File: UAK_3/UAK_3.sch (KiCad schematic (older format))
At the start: 57 parts, among them K1 Кнопка_FSMSM, K2 Кнопка_FSMSM, X1 Крепежное_отверстие_М3, X2 Крепежное_отверстие_М3, X3 Крепежное_отверстие_М3, X4 Крепежное_отверстие_М3

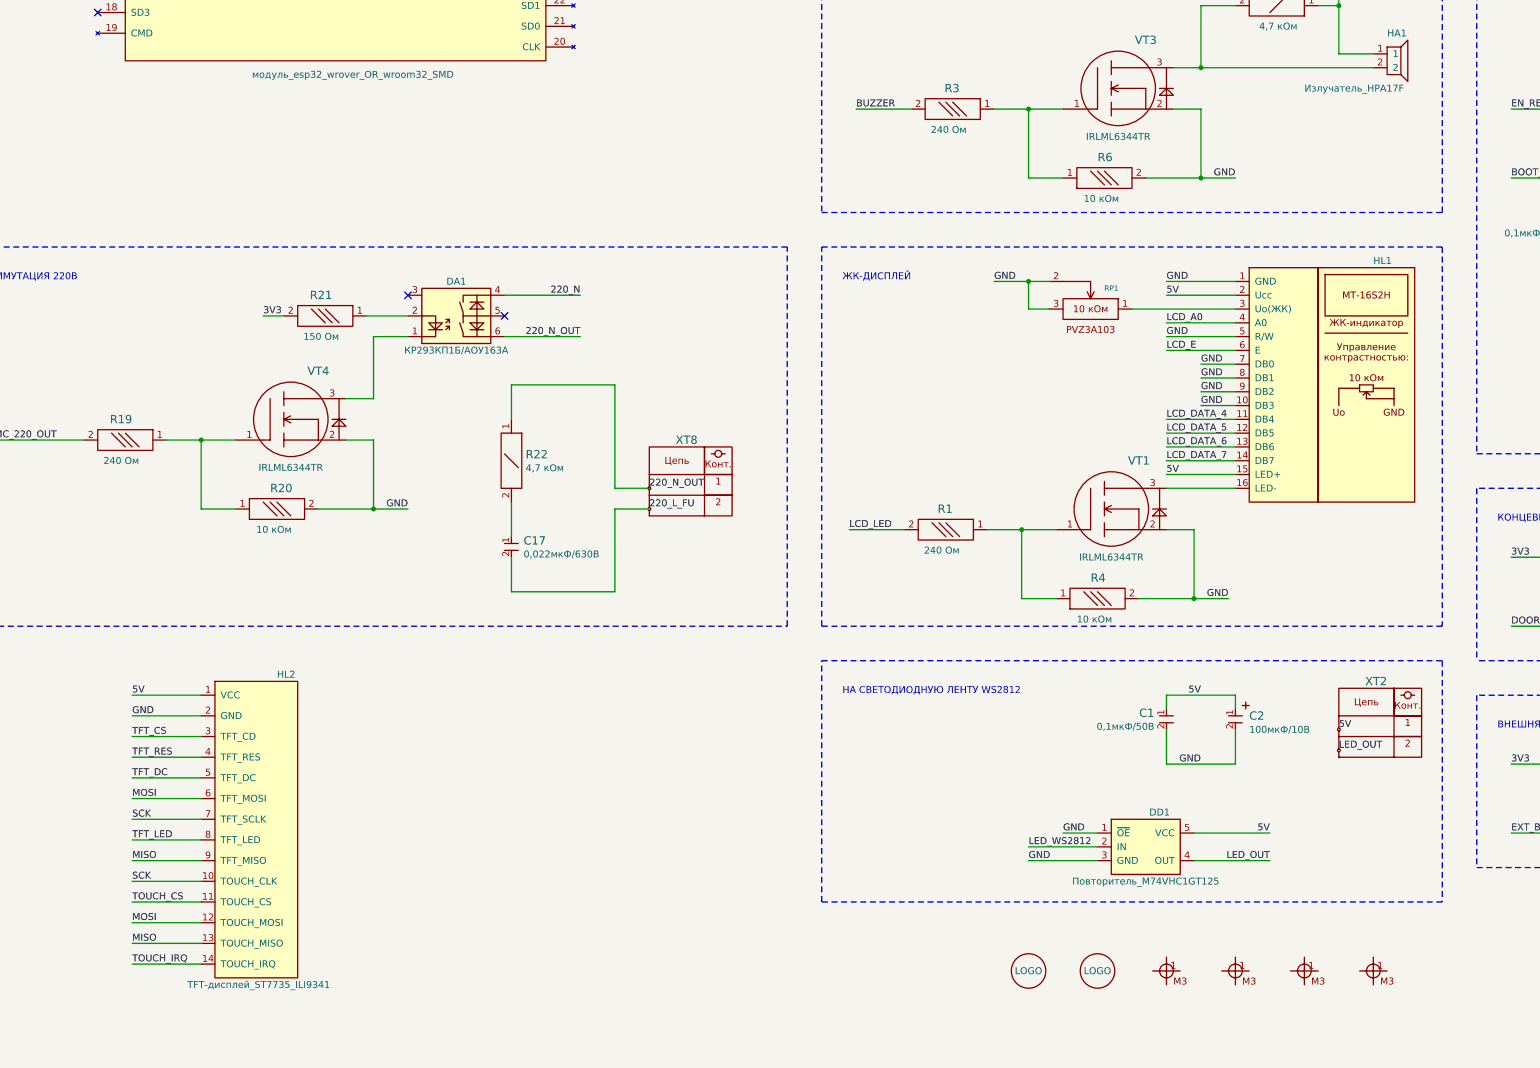
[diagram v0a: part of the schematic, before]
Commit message: добавлены сопротивления: в управление ЖК и выход 220
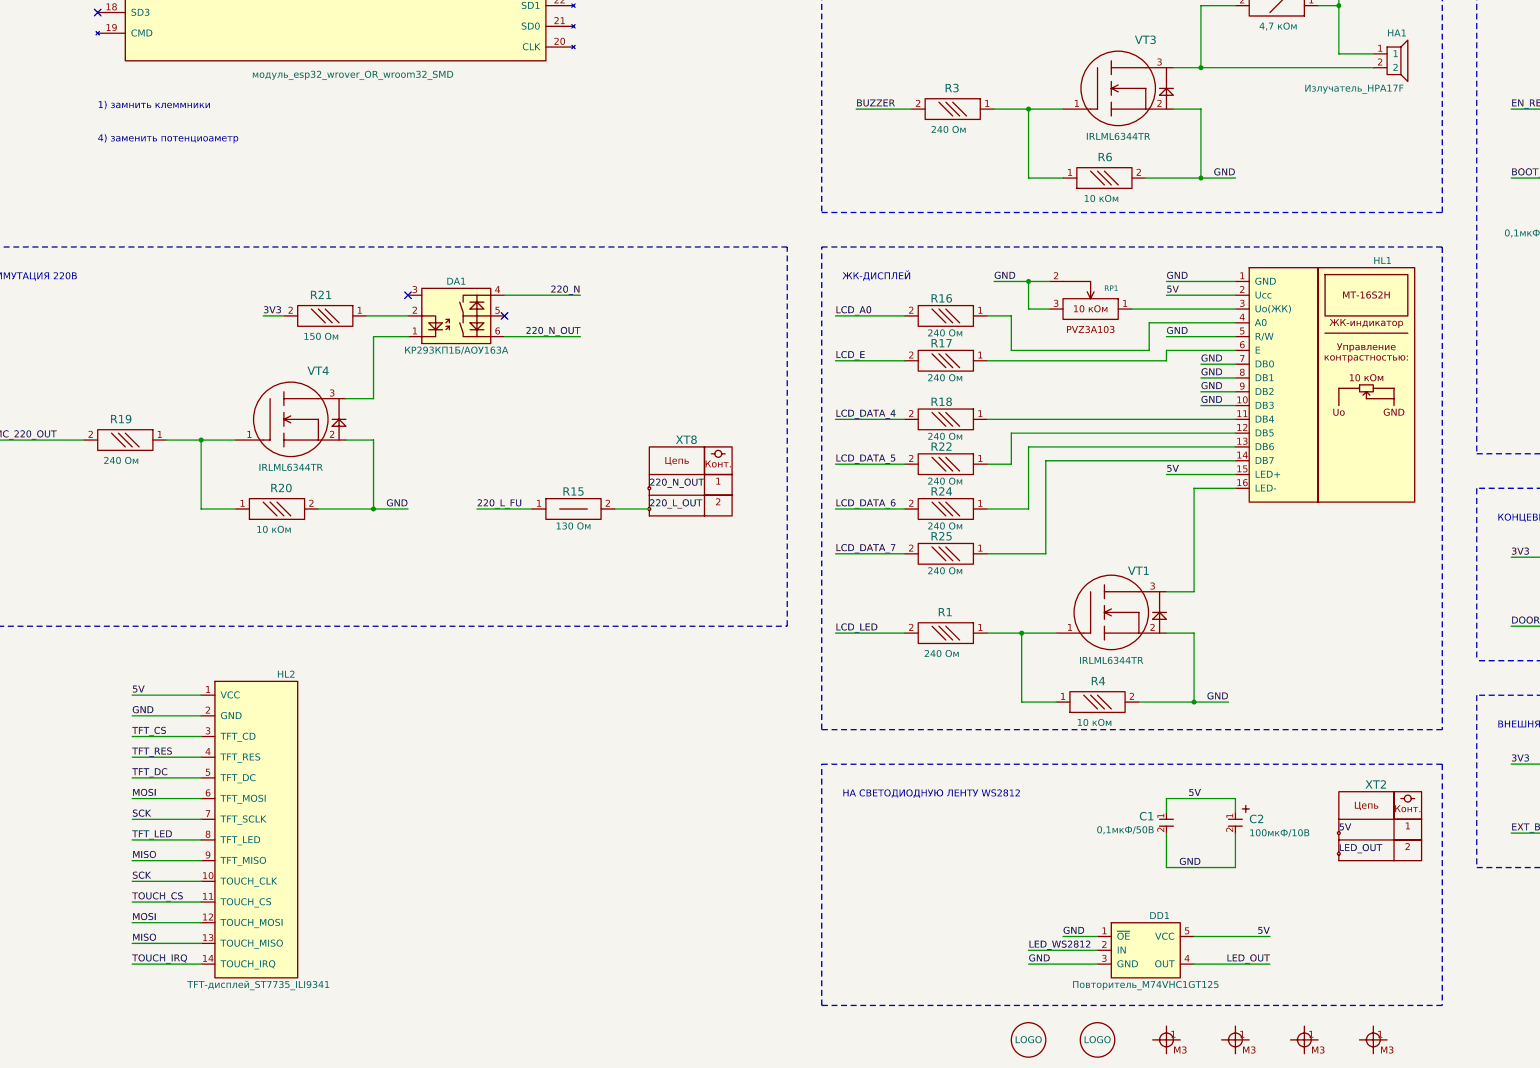
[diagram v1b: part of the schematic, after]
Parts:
- removed C17: Конденсатор_керамический, N_RLC:Конденсатор_SMD_1210, symbol elements:Конденсатор_керамический
- removed R22: Резистор_0,25Вт, N_RLC:Резистор_SMD_1206-0,25_Вт, symbol elements:Резистор_0,25Вт
- added R15: Резистор_0,5Вт, N_RLC:Резистор_SMD_2010-0,5_Вт, symbol elements:Резистор_0,5Вт
- added R16, R17, R18, R22, R24, R25: Резистор_0,065Вт, N_RLC:Резистор_SMD_0603_0,065_Вт, symbol elements:Резистор_0,065Вт
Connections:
- net 220_L_FU: now also R15.1; no longer XT8.2
- net LCD_A0: now also R16.2; no longer HL1.4 (A0)
- net LCD_DATA_4: now also R18.2; no longer HL1.11 (DB4)
- net LCD_DATA_5: now also R22.2; no longer HL1.12 (DB5)
- net LCD_DATA_6: now also R24.2; no longer HL1.13 (DB6)
- net LCD_DATA_7: now also R25.2; no longer HL1.14 (DB7)
- net LCD_E: now also R17.2; no longer HL1.6 (E)
- new net: HL1.11 (DB4), R18.1
- new net: HL1.12 (DB5), R22.1
- new net: HL1.13 (DB6), R24.1
- new net: HL1.14 (DB7), R25.1
- new net: HL1.4 (A0), R16.1
- new net: HL1.6 (E), R17.1
- new net 220_L_OUT: R15.2, XT8.2
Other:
- note added: "1) замнить клеммники\n\n\n4) заменить потенциоаметр"
- moved on the sheet: C1, C2, DD1, R1, R4, VT1, XT2

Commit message: заменены клеммники
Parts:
- removed XT1, XT2, XT3, XT6, XT7: Клеммник_х2_308-021-14, N_X:Клеммник_х2_шаг2.54, symbol UAK_3-rescue:Клеммник_х2_KLS2-300-5.00-02P-2S-elements_2020-UAK_0-rescue-UAK_1-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
- removed XT4, XT8: Клеммник_х2_KLS2-300-5.00-02P-2S, N_X:Клеммник_х2_шаг5, symbol UAK_3-rescue:Клеммник_х2_KLS2-300-5.00-02P-2S-elements_2020-UAK_0-rescue-UAK_1-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
- added X5: Клеммник_х4, N_X:Клеммник_х4_шаг3,81_15EDGRC, symbol elements:Клеммник_х4
- added X6: Клеммник_х10, N_X:Клеммник_х10_шаг3,81_15EDGRC, symbol elements:Клеммник_х10
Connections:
- net 220_L: now also X5.3
- net 220_L_OUT: now also X5.2
- net 220_N: now also X5.4
- net 220_N_OUT: now also X5.1
- net 5V: now also X6.3, X6.8, X6.9
- net BUTT_1: now also X6.6
- net DOOR_1: now also X6.1
- net D_OUT_1: now also X6.10
- net GND: now also X6.2, X6.5, X6.7
- net LED_OUT: now also X6.4
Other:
- note added: "4) заменить потенциометр"
- note added: "ПОДСВЕТКА ЛАМПЫ \n(ОТКРЫТЫЙ СТОК)"
- note removed: "1) замнить клеммники\n\n\n4) заменить потенциоаметр"
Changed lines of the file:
@@
 EESchema Schematic File Version 4
 LIBS:UAK_3-cache
-EELAYER 30 0
+EELAYER 29 0
 EELAYER END
 $Descr A3 16535 11693
@@
 	1    1950 1000
 	1    0    0    -1
-$EndComp
-$Comp
-L UAK_3-rescue:Клеммник_х2_KLS2-300-5.00-02P-2S-elements_2020-UAK_0-rescue-UAK_1-rescue-UAK_2-rescue XT4
-U 1 1 5F53E542
-P 14750 1500
-F 0 "XT4" H 14400 1850 60  0000 L CNN
-F 1 "Клеммник_х2_KLS2-300-5.00-02P-2S" H 14440 1240 60  0001 C CNN
-F 2 "N_X:Клеммник_х2_шаг5" H 14175 1775 60  0001 C CNN
-F 3 "" H 14175 1775 60  0001 C CNN
-F 4 "https://www.chipdip.ru/product/kls2-300-5.00-02p-2s-dg300-5.0-02p-12" H 14750 1500 50  0001 C CNN "LINK"
-F 5 "Клеммник KLS2-300-5.00-02P-2S (шаг 5 мм)" H 14750 1500 50  0001 C CNN "Для заказа"
-	1    14750 1500
-	-1   0    0    -1
 $EndComp
 Text Label 14750 1500 0    50   ~ 0
@@
 	-1   0    0    -1
 $EndComp
-Text Label 14750 8000 2    50   ~ 0
+Text Label 14250 8000 2    50   ~ 0
 GND
 $Comp
@@
 Wire Wire Line
 	13000 8000 13000 7500
-$Comp
-L UAK_3-rescue:Клеммник_х2_KLS2-300-5.00-02P-2S-elements_2020-UAK_0-rescue-UAK_1-rescue-UAK_2-rescue XT6
-U 1 1 5F598429
-P 14500 7500
-F 0 "XT6" H 14150 7850 60  0000 L CNN
-F 1 "Клеммник_х2_308-021-14" H 14190 7240 60  0001 C CNN
-F 2 "N_X:Клеммник_х2_шаг2.54" H 13925 7775 60  0001 C CNN
-F 3 "" H 13925 7775 60  0001 C CNN
-F 4 "https://www.chipdip.ru/product/308-021-12-14" H 14500 7500 50  0001 C CNN "LINK"
-F 5 "Клеммник 308-021-14 (шаг 2,54 мм)" H 14500 7500 50  0001 C CNN "Для заказа"
-	1    14500 7500
-	-1   0    0    -1
-$EndComp
 Connection ~ 13000 8000
-Wire Wire Line
-	13850 7500 14500 7500
-Wire Wire Line
-	14250 8000 14250 7650
-Wire Wire Line
-	14250 7650 14500 7650
-Wire Wire Line
-	13650 8000 14250 8000
-Wire Wire Line
-	14250 8000 14750 8000
-Connection ~ 14250 8000
-Text Label 14500 7500 0    50   ~ 0
+Text Label 14250 7500 2    50   ~ 0
 DOOR_1
 Wire Notes Line
@@
 Text Label 7250 2000 0    50   ~ 0
 MC_OUT_1
-Text Label 10750 1700 0    50   ~ 0
+Text Label 10250 1700 2    50   ~ 0
 D_OUT_1
 Wire Wire Line
@@
 Text Label 10000 2500 2    50   ~ 0
 GND
-$Comp
-L UAK_3-rescue:Клеммник_х2_KLS2-300-5.00-02P-2S-elements_2020-UAK_0-rescue-UAK_1-rescue-UAK_2-rescue XT1
-U 1 1 5F5B9CF4
-P 10750 1550
-F 0 "XT1" H 10400 1900 60  0000 L CNN
-F 1 "Клеммник_х2_308-021-14" H 10440 1290 60  0001 C CNN
-F 2 "N_X:Клеммник_х2_шаг2.54" H 10175 1825 60  0001 C CNN
-F 3 "" H 10175 1825 60  0001 C CNN
-F 4 "https://www.chipdip.ru/product/308-021-12-14" H 10750 1550 50  0001 C CNN "LINK"
-F 5 "Клеммник 308-021-14 (шаг 2,54 мм)" H 10750 1550 50  0001 C CNN "Для заказа"
-	1    10750 1550
-	-1   0    0    -1
-$EndComp
 $Comp
 L UAK_3-rescue:Диод_шоттки_SK16-elements_2020-UAK_0-rescue-UAK_1-rescue-UAK_2-rescue VD1
@@
 Wire Wire Line
 	9750 1500 9750 1700
-Connection ~ 9750 1700
-Wire Wire Line
-	9750 1700 10750 1700
 Text Notes 7150 1000 0    50   ~ 0
 ПОДСВЕТКА ЛАМПЫ (ОТКРЫТЫЙ СТОК)
@@
 	-1   0    0    -1
 $EndComp
-Text Label 14750 9500 2    50   ~ 0
+Text Label 14250 9500 2    50   ~ 0
 GND
 $Comp
@@
 Wire Wire Line
 	13000 9500 13000 9000
-$Comp
-L UAK_3-rescue:Клеммник_х2_KLS2-300-5.00-02P-2S-elements_2020-UAK_0-rescue-UAK_1-rescue-UAK_2-rescue XT7
-U 1 1 5F5BFDD6
-P 10750 2250
-F 0 "XT7" H 10400 2600 60  0000 L CNN
-F 1 "Клеммник_х2_308-021-14" H 10440 1990 60  0001 C CNN
-F 2 "N_X:Клеммник_х2_шаг2.54" H 10175 2525 60  0001 C CNN
-F 3 "" H 10175 2525 60  0001 C CNN
-F 4 "https://www.chipdip.ru/product/308-021-12-14" H 10750 2250 50  0001 C CNN "LINK"
-F 5 "Клеммник 308-021-14 (шаг 2,54 мм)" H 10750 2250 50  0001 C CNN "Для заказа"
-	1    10750 2250
-	-1   0    0    -1
-$EndComp
 Connection ~ 13000 9500
-Text Label 14500 9150 0    50   ~ 0
-BUTT_1
 Wire Notes Line
 	11750 9750 15500 9750
@@
 Wire Wire Line
 	5200 1400 5750 1400
-$Comp
-L UAK_3-rescue:Клеммник_х2_KLS2-300-5.00-02P-2S-elements_2020-UAK_0-rescue-UAK_1-rescue-UAK_2-rescue XT2
-U 1 1 5F79F40F
-P 10750 9500
-F 0 "XT2" H 10400 9850 60  0000 L CNN
-F 1 "Клеммник_х2_308-021-14" H 10440 9240 60  0001 C CNN
-F 2 "N_X:Клеммник_х2_шаг2.54" H 10175 9775 60  0001 C CNN
-F 3 "" H 10175 9775 60  0001 C CNN
-F 4 "https://www.chipdip.ru/product/308-021-12-14" H 10750 9500 50  0001 C CNN "LINK"
-F 5 "Клеммник 308-021-14 (шаг 2,54 мм)" H 10750 9500 50  0001 C CNN "Для заказа"
-	1    10750 9500
-	-1   0    0    -1
-$EndComp
-$Comp
-L UAK_3-rescue:Клеммник_х2_KLS2-300-5.00-02P-2S-elements_2020-UAK_0-rescue-UAK_1-rescue-UAK_2-rescue XT3
-U 1 1 5F7A0B62
-P 14500 9000
-F 0 "XT3" H 14150 9350 60  0000 L CNN
-F 1 "Клеммник_х2_308-021-14" H 14190 8740 60  0001 C CNN
-F 2 "N_X:Клеммник_х2_шаг2.54" H 13925 9275 60  0001 C CNN
-F 3 "" H 13925 9275 60  0001 C CNN
-F 4 "https://www.chipdip.ru/product/308-021-12-14" H 14500 9000 50  0001 C CNN "LINK"
-F 5 "Клеммник 308-021-14 (шаг 2,54 мм)" H 14500 9000 50  0001 C CNN "Для заказа"
-	1    14500 9000
-	-1   0    0    -1
-$EndComp
-Text Label 10750 2250 0    50   ~ 0
-GND
 Text Label 10250 10450 2    50   ~ 0
 LED_OUT
 Wire Wire Line
 	9700 10450 10250 10450
-Text Label 10750 9500 0    50   ~ 0
-5V
-Text Label 10750 9650 0    50   ~ 0
-LED_OUT
 Wire Notes Line
 	11500 9000 11500 10750
@@
 Text Notes 7150 9250 0    50   ~ 0
 НА СВЕТОДИОДНУЮ ЛЕНТУ WS2812
-$Comp
-L UAK_3-rescue:Клеммник_х2_KLS2-300-5.00-02P-2S-elements_2020-UAK_0-rescue-UAK_1-rescue-UAK_2-rescue XT8
-U 1 1 5F5696D9
-P 5750 7000
-F 0 "XT8" H 5400 7350 60  0000 L CNN
-F 1 "Клеммник_х2_KLS2-300-5.00-02P-2S" H 5440 6740 60  0001 C CNN
-F 2 "N_X:Клеммник_х2_шаг5" H 5175 7275 60  0001 C CNN
-F 3 "" H 5175 7275 60  0001 C CNN
-F 4 "https://www.chipdip.ru/product/kls2-300-5.00-02p-2s-dg300-5.0-02p-12" H 5750 7000 50  0001 C CNN "LINK"
-F 5 "Клеммник KLS2-300-5.00-02P-2S (шаг 5 мм)" H 5750 7000 50  0001 C CNN "Для заказа"
-	1    5750 7000
-	-1   0    0    -1
-$EndComp
 $Comp
 L UAK_3-rescue:МОП-реле_КР293КП1Б-elements_2020-UAK_0-rescue-UAK_1-rescue-UAK_2-rescue DA1
@@
 Text Label 5250 5900 2    50   ~ 0
 220_N_OUT
-Text Label 5750 7000 0    50   ~ 0
+Text Label 5000 9000 2    50   ~ 0
 220_N_OUT
 $Comp
@@
 Wire Wire Line
 	4700 5900 5250 5900
-Text Label 14500 7650 0    50   ~ 0
-GND
-Text Label 14500 9000 0    50   ~ 0
-GND
 $Comp
 L elements:Резистор_0,25Вт R23
@@
 	1    0    0    -1
 $EndComp
-Wire Wire Line
-	13650 9500 14250 9500
-Wire Wire Line
-	13850 9000 14000 9000
-Wire Wire Line
-	14000 9150 14500 9150
-Wire Wire Line
-	14000 9000 14000 9150
-Wire Wire Line
-	14500 9000 14250 9000
-Wire Wire Line
-	14250 9000 14250 9500
-Connection ~ 14250 9500
-Wire Wire Line
-	14250 9500 14750 9500
-Text Label 10750 2400 0    50   ~ 0
-5V
 $Comp
 L UAK_3-rescue:Держатель_предохранителя_KLS5-266-elements_2020-UAK_1-rescue-UAK_2-rescue XFU1
@@
 Wire Wire Line
 	5200 3350 6250 3350
-Text Label 10750 1550 0    50   ~ 0
-5V
 Text Label 9750 1000 0    50   ~ 0
 5V
 NoConn ~ 1750 2950
 Text Notes 1750 4500 0    50   ~ 0
-1) замнить клеммники\n\n\n4) заменить потенциоаметр
+4) заменить потенциометр
 $Comp
 L elements:Резистор_0,5Вт R15
@@
 Wire Wire Line
 	4500 7150 4900 7150
-Wire Wire Line
-	5500 7150 5750 7150
-Text Label 5750 7150 0    50   ~ 0
+Text Label 5000 9150 2    50   ~ 0
 220_L_OUT
 $Comp
@@
 Wire Wire Line
 	9375 5800 10000 5800
+$Comp
+L elements:Клеммник_х10 X6
+U 1 1 6086F8F7
+P 6000 9000
+F 0 "X6" H 5450 9350 60  0000 L CNN
+F 1 "Клеммник_х10" H 5750 7500 60  0001 C CNN
+F 2 "N_X:Клеммник_х10_шаг3,81_15EDGRC" H 5425 9275 60  0001 C CNN
+F 3 "" H 5425 9275 60  0001 C CNN
+	1    6000 9000
+	1    0    0    -1
+$EndComp
+$Comp
+L elements:Клеммник_х4 X5
+U 1 1 60875B82
+P 5000 9000
+F 0 "X5" H 4450 9350 60  0000 L CNN
+F 1 "Клеммник_х4" H 4800 8450 60  0001 C CNN
+F 2 "N_X:Клеммник_х4_шаг3,81_15EDGRC" H 4425 9275 60  0001 C CNN
+F 3 "" H 4425 9275 60  0001 C CNN
+	1    5000 9000
+	1    0    0    -1
+$EndComp
+Text Label 5000 9300 2    50   ~ 0
+220_L
+Text Label 5000 9450 2    50   ~ 0
+220_N
+Text Label 6000 7150 2    50   ~ 0
+220_L_OUT
+Wire Wire Line
+	5500 7150 6000 7150
+Text Label 6000 9000 2    50   ~ 0
+DOOR_1
+Text Label 6000 9150 2    50   ~ 0
+GND
+Wire Wire Line
+	14250 7500 13850 7500
+Wire Wire Line
+	14250 8000 13650 8000
+Text Label 6000 9300 2    50   ~ 0
+5V
+Text Label 6000 9450 2    50   ~ 0
+LED_OUT
+Text Label 6000 9600 2    50   ~ 0
+GND
+Text Label 6000 9750 2    50   ~ 0
+BUTT_1
+Wire Wire Line
+	14250 9500 13650 9500
+Wire Wire Line
+	13850 9000 14250 9000
+Text Label 14250 9000 2    50   ~ 0
+BUTT_1
+Text Label 6000 9900 2    50   ~ 0
+GND
+Text Label 6000 10050 2    50   ~ 0
+5V
+Text Notes 6200 10550 1    50   ~ 0
+ПОДСВЕТКА ЛАМПЫ \n(ОТКРЫТЫЙ СТОК)
+Text Label 6000 10200 2    50   ~ 0
+5V
+Text Label 6000 10350 2    50   ~ 0
+D_OUT_1
+Wire Wire Line
+	10250 1700 9750 1700
+Connection ~ 9750 1700
 $EndSCHEMATC
